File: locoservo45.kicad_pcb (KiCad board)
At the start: 2 copper layers, 21 parts, among them J1 RJ45, J10 Srv3_1, J11 Srv4_2, J12 Srv4_1, J13 Var1, J14 Var2, J15 Var3, J16 Var4, J2 RJ45, J3 RJ45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

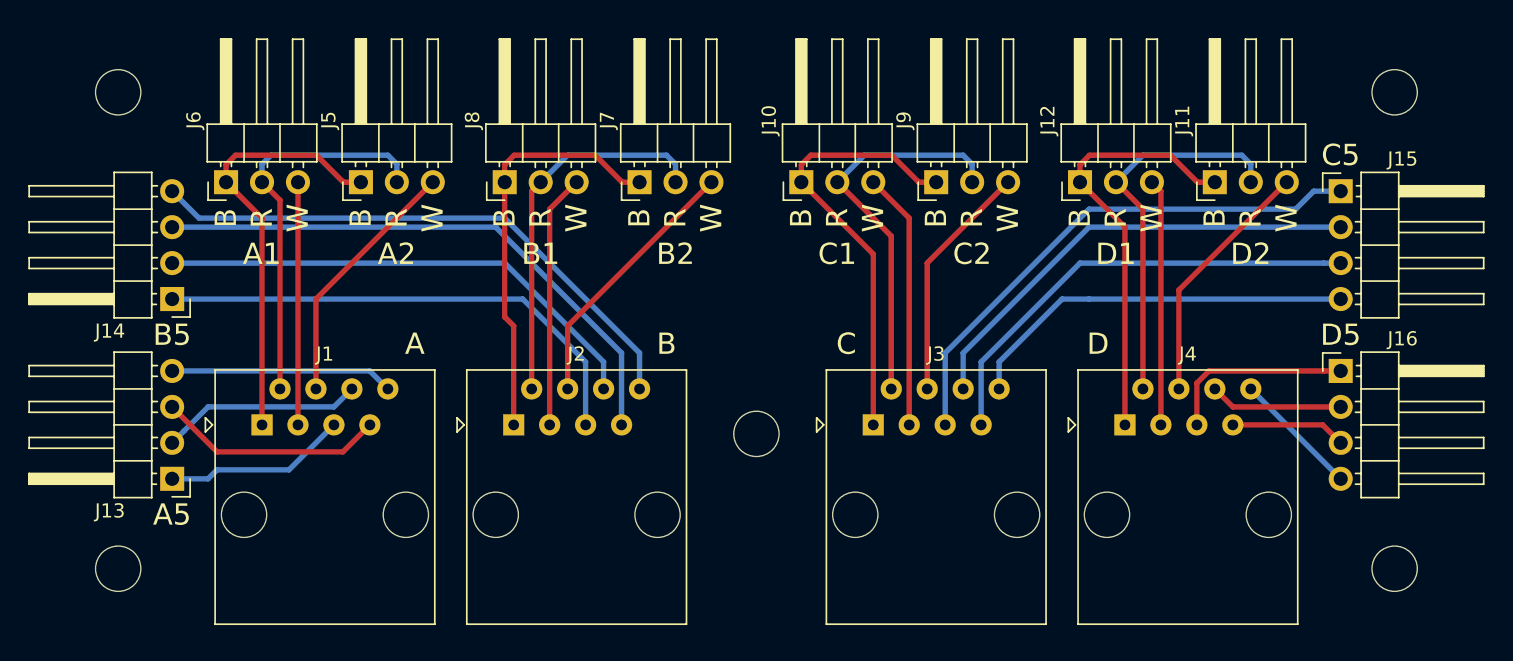
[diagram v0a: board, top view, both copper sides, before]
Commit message: Add edge cuts; Fix mounting holes
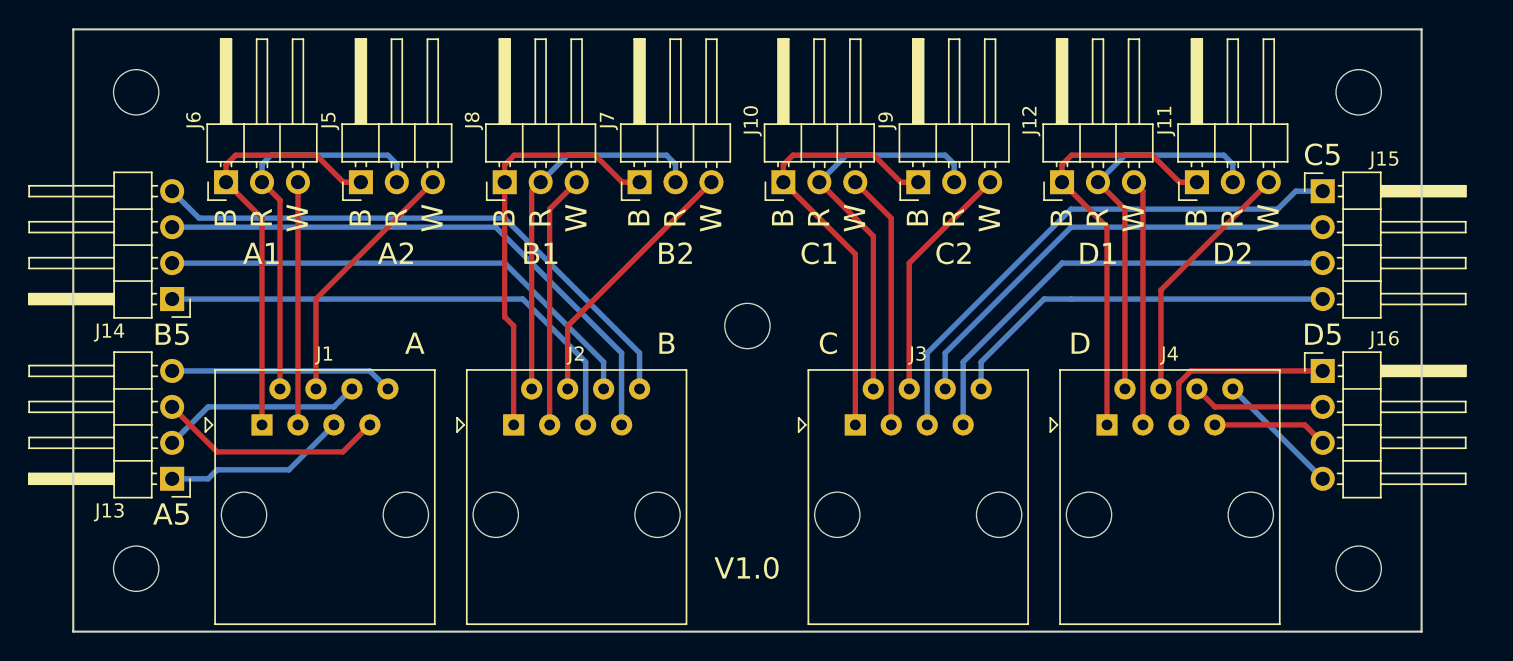
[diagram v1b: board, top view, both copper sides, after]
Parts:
- moved ? 7.65 mm to (139.7, 111.1)
- moved ? 2.54 mm to (182.9, 128.3)
- moved ? 2.54 mm to (182.9, 94.6)
- moved J11 1.27 mm to (171.4, 101.0)
- moved J15 1.27 mm to (180.3, 101.6)
- moved J16 1.27 mm to (180.3, 114.3)
- moved J3 1.27 mm to (147.3, 118.1)
- moved J4 1.27 mm to (165.1, 118.1)
- moved J9 1.27 mm to (151.8, 101.0)
- moved ? 1.27 mm to (96.5, 128.3)
- moved ? 1.27 mm to (96.5, 94.6)
- moved J10 1.27 mm to (142.2, 101.0)
- moved J12 1.27 mm to (161.9, 101.0)
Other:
- board outline added: 95.2 x 42.5 mm
- board text added: "V1.0"
